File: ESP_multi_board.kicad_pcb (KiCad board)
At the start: 2 copper layers, 100 x 50 mm, 57 parts, among them IC101 L298, P101 CONN_01X02, P102 CONN_01X06, P103 CONN_01X02, P104 CONN_01X06, P105 CONN_01X06, P106 CONN_01X03, P107 CONN_I2C_MPU6050, P108 CONN_PINES_DIG, P109 CONN_01X04, SW101 SW_PUSH_SMALL, SW102 SWITCH_INV, U1 LD1117S33TR, U102 ESP-12, U103 MAX11605EEE+, U104 MCP23008

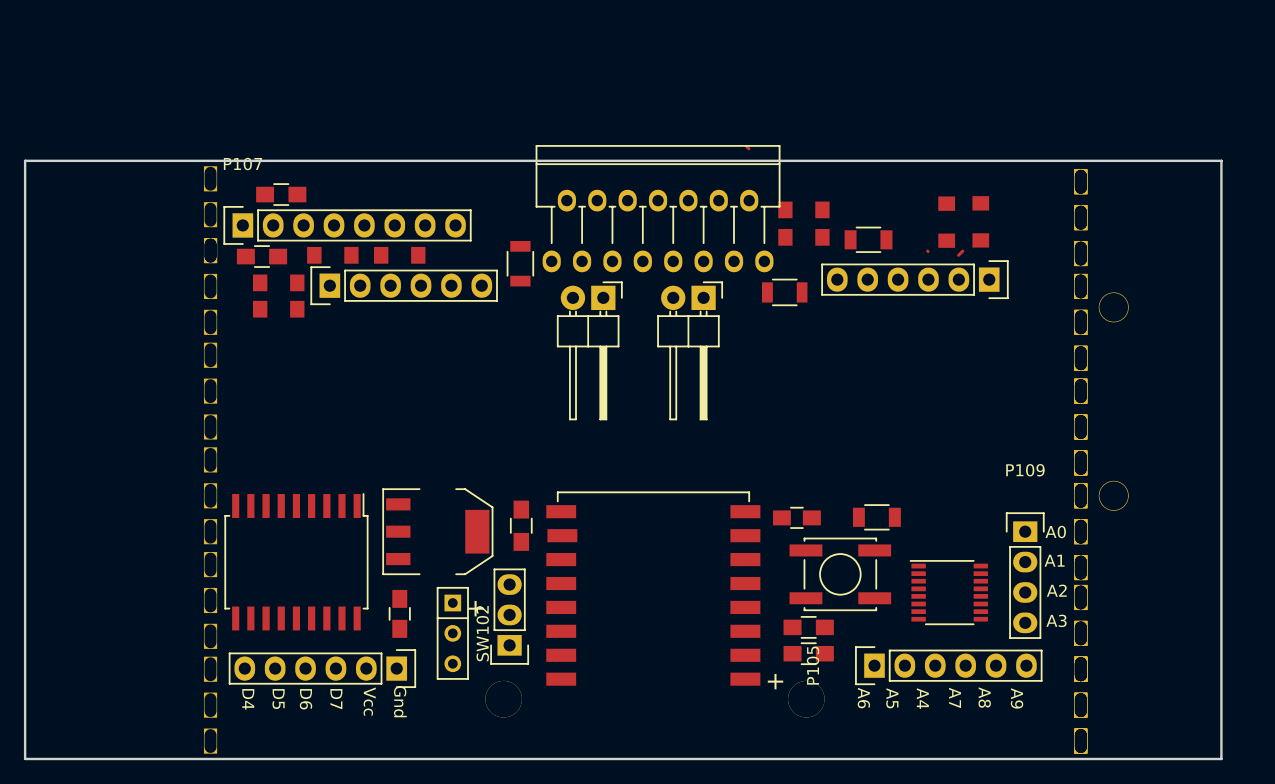
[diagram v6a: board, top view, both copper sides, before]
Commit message: placa final con doble agujeros (sin doble troquel)
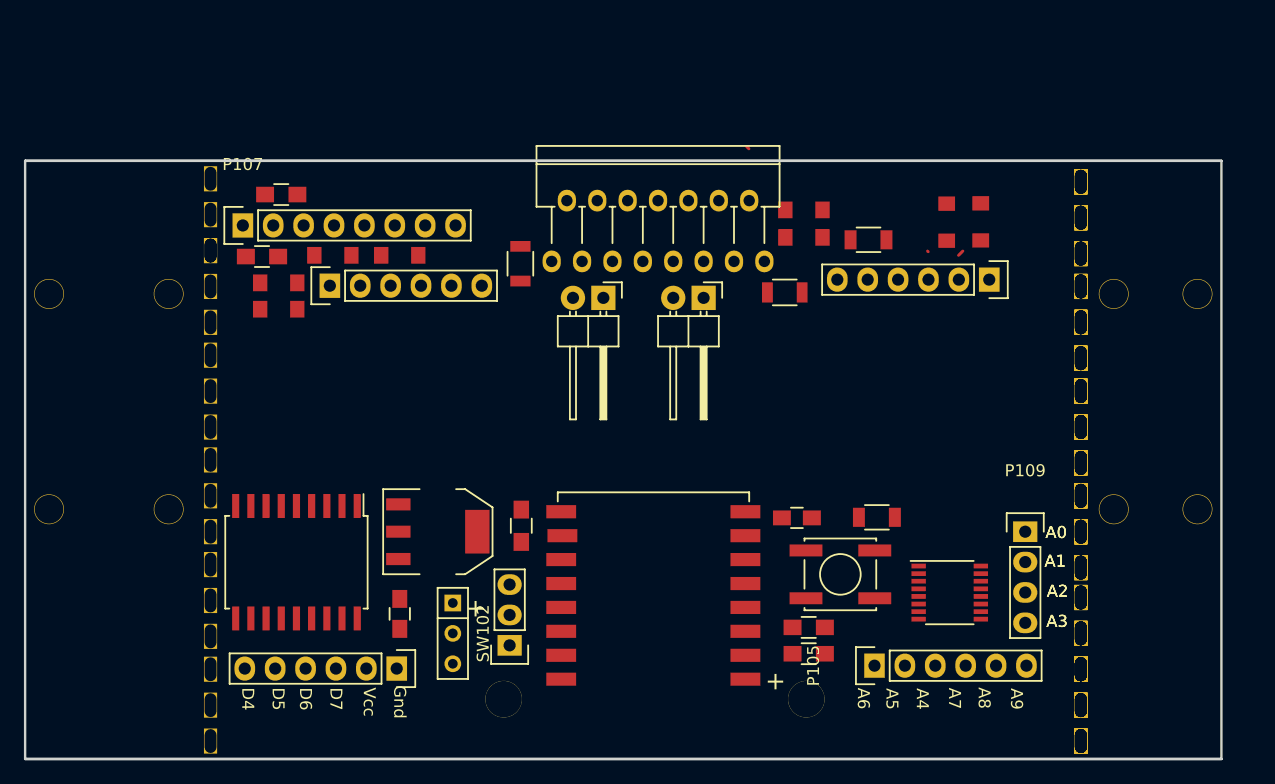
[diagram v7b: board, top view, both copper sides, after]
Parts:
- added REF**: 1pin, Connect:1pin, F.Cu at (86.0, 93.0)
- added REF** (x2): troquel, taladros:troquel_3, F.Cu at (172.2, 87.2)
- added REF** (x2): troquel, taladros:troquel_3, F.Cu at (172.2, 78.5)
- added REF** (x2): troquel, taladros:troquel_3, F.Cu at (172.2, 69.8)
- added REF** (x2): troquel, taladros:troquel_3, F.Cu at (172.2, 110.5)
- added REF** (x2): troquel, taladros:troquel_3, F.Cu at (172.2, 104.5)
- added REF** (x2): troquel, taladros:troquel_3, F.Cu at (172.2, 96.0)
- added REF**: 1pin, Connect:1pin, F.Cu at (86.0, 77.2)
- added REF**: 1pin, Connect:1pin, F.Cu at (96.0, 77.2)
- added REF**: 1pin, Connect:1pin, F.Cu at (96.0, 93.0)
- added REF**: 1pin, Connect:1pin, F.Cu at (182.0, 93.0)
- added REF**: 1pin, Connect:1pin, F.Cu at (182.0, 75.0)

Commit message: limpiada (dobles elementos) y con refeencias unicas
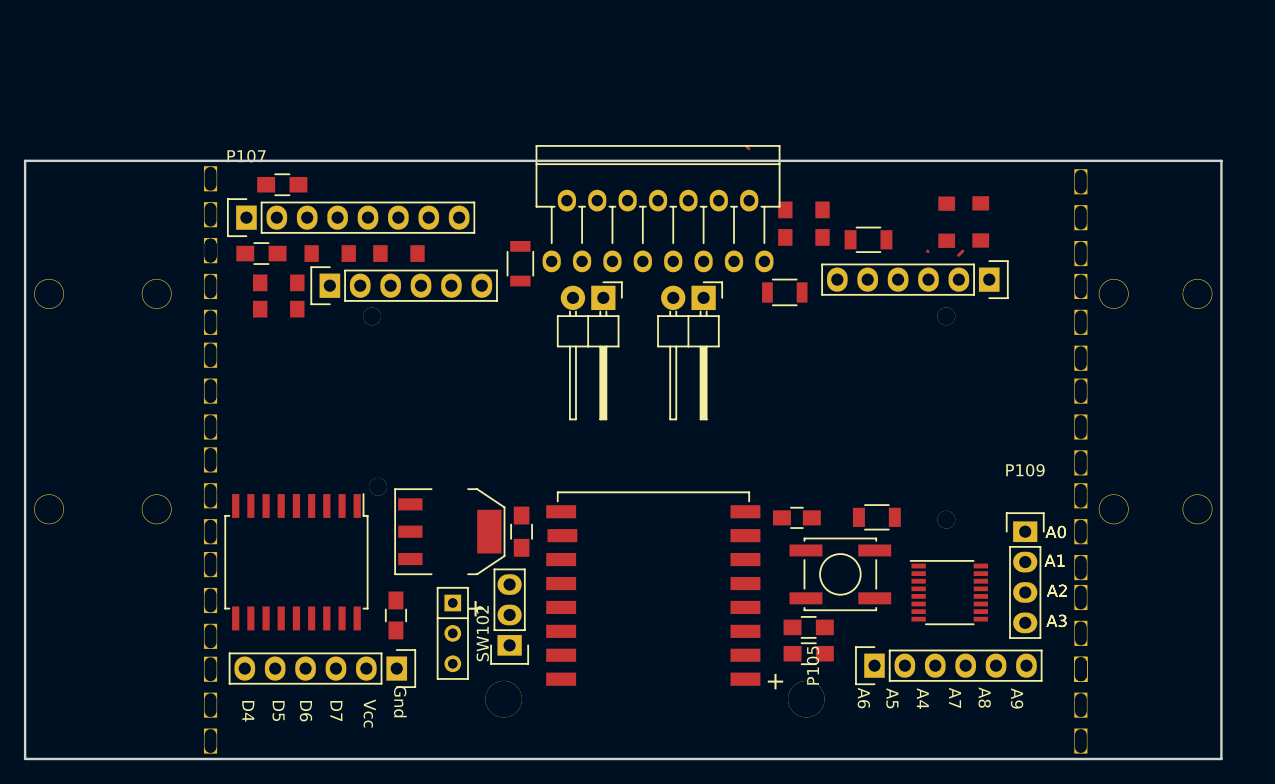
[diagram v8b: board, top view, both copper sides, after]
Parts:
- removed REF** (x18): troquel, taladros:troquel_3
- added drill20: 1pin, Connect:1pin, F.Cu at (113.0, 78.0)
- added drill5: 1pin, Connect:1pin, F.Cu at (161.0, 78.0)
- added drill6: 1pin, Connect:1pin, F.Cu at (161.0, 95.0)
- added drill9: 1pin, Connect:1pin, F.Cu at (113.5, 92.2)
- moved U1 1.00 mm to (119.5, 96.0)
- moved R105 0.82 mm to (105.5, 67.0)
- moved P107 0.72 mm to (102.5, 69.8)
- moved R103 0.50 mm to (125.5, 96.0)
- moved C2 0.34 mm to (115.0, 103.0)
- moved D103 0.27 mm to (109.5, 72.8)
- moved R104 0.25 mm to (103.8, 72.8)
- moved D104 0.16 mm to (115.2, 72.8)
- renumbered REF** to drill1, REF** to drill11, REF** to drill12, REF** to drill13, REF** to drill14, REF** to drill2, REF** to drill3, REF** to drill4, REF** to drill7, REF** to drill8, REF** to troqel1, REF** to troqel2, REF** to troquel11, REF** to troquel12, REF** to troquel13, REF** to troquel14, REF** to troquel15, REF** to troquel16, REF** to troquel3, REF** to troquel4, REF** to troquel5, REF** to troquel6
